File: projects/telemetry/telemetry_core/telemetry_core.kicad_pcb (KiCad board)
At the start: 2 copper layers, 76.2 x 63.5 mm, 59 parts, among them J1 MM_F_RA_20, J2 JST_SM06B-GHS-TB_LF__SN_, J3 CONN_02X03, U1 ATMEGA16M1, U2 TPS560430YF, U3 MCP79511-I_MS, U4 TXB0104PW, U5 LM3480-3.3, U6 MCP2561-E_SN, Y1 Crystal_SMD, Y2 Crystal_32_768kHz

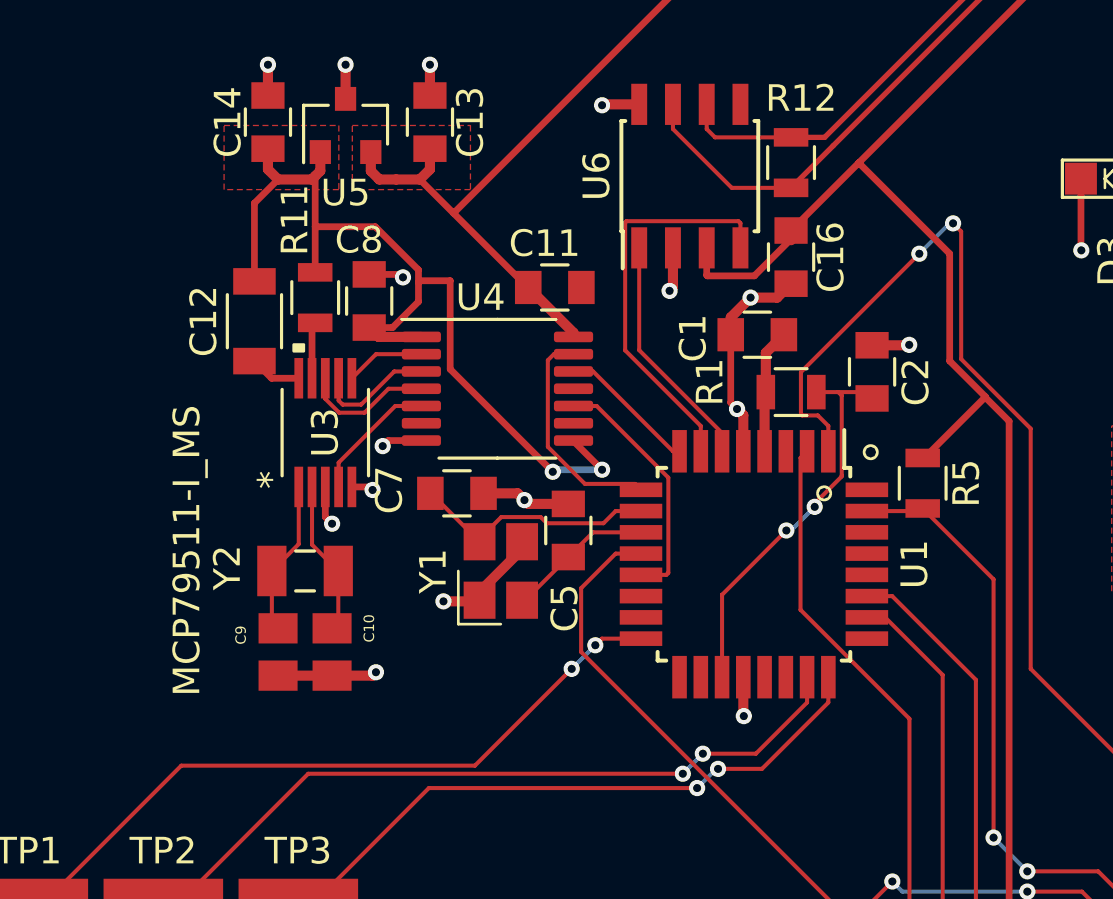
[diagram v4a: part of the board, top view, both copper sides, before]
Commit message: fix: add missing connections, hide label
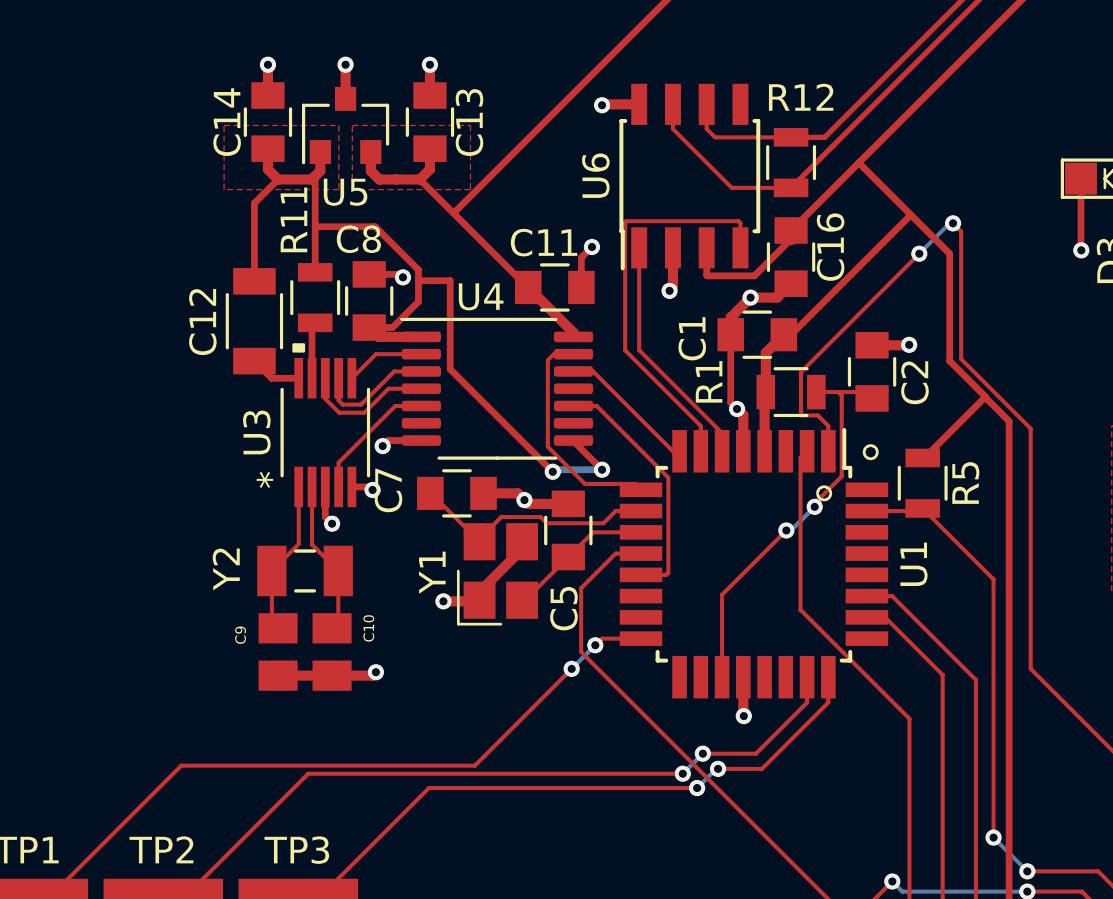
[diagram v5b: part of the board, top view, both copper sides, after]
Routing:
- net +5V: track 137.0 -> 143.6 mm
- net GND: track 98.9 -> 100.6 mm, vias 35 -> 36
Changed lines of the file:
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@@
     (thickness 1.6)
     (drawings 36)
-    (tracks 463)
+    (tracks 469)
     (zones 0)
     (modules 59)
@@
   )
   (setup
-    (last_trace_width 0.1524)
+    (last_trace_width 0.254)
     (user_trace_width 0.254)
     (user_trace_width 0.381)
@@
     (tags "capacitor 0805")
     (attr smd)
-    (fp_text reference C16 (at 0 -1.5 90) (layer F.SilkS)
+    (fp_text reference C16 (at -0.381 -1.524 90) (layer F.SilkS)
       (effects (font (size 1 1) (thickness 0.15)))
     )
@@
       (effects (font (size 1 1) (thickness 0.15)))
     )
-    (fp_text value JST_SM06B-GHS-TB_LF__SN_ (at 9.525 3.84 270) (layer F.Fab)
+    (fp_text value JST_SM06B-GHS-TB_LF__SN_ (at 6.731 -9.652 270) (layer F.Fab)
       (effects (font (size 1 1) (thickness 0.15)))
     )
@@
     (tags "rtc, spi, clock, clk")
     (attr smd)
-    (fp_text reference U3 (at 0 0 90) (layer F.SilkS)
+    (fp_text reference U3 (at 0 -2.54 90) (layer F.SilkS)
       (effects (font (size 1 1) (thickness 0.15)))
     )
-    (fp_text value MCP79511-I_MS (at -4.445 -5.207 90) (layer F.SilkS)
+    (fp_text value MCP79511-I_MS (at -4.445 -5.207 90) (layer F.SilkS) hide
       (effects (font (size 1 1) (thickness 0.15)))
     )
@@
   (via (at 131.699 112.141) (size 0.6096) (drill 0.3048) (layers F.Cu B.Cu) (net 1))
   (segment (start 131.699 113.3) (end 131.699 112.141) (width 0.381) (layer F.Cu) (net 1))
+  (via (at 143.891 118.999) (size 0.6096) (drill 0.3048) (layers F.Cu B.Cu) (net 1))
+  (segment (start 143.494 119.396) (end 143.891 118.999) (width 0.254) (layer F.Cu) (net 1))
+  (segment (start 143.494 120.523) (end 143.494 119.396) (width 0.254) (layer F.Cu) (net 1))
   (segment (start 172.614 102.637) (end 172.593 102.616) (width 0.381) (layer F.Cu) (net 2))
   (segment (start 172.593 112.374) (end 172.614 112.395) (width 0.381) (layer F.Cu) (net 2))
@@
   (segment (start 150.002521 120.086401) (end 148.234401 120.086401) (width 0.254) (layer F.Cu) (net 3))
   (segment (start 151.384 118.38) (end 151.384 118.704922) (width 0.254) (layer F.Cu) (net 3))
-  (segment (start 153.932 115.832) (end 157.353 119.253) (width 0.254) (layer F.Cu) (net 3))
   (segment (start 160.798 108.966) (end 153.932 115.832) (width 0.254) (layer F.Cu) (net 3))
   (segment (start 153.932 115.832) (end 151.384 118.38) (width 0.254) (layer F.Cu) (net 3))
@@
   (segment (start 150.622 105.791) (end 138.684 117.729) (width 0.254) (layer F.Cu) (net 3))
   (segment (start 138.684 117.729) (end 137.414 116.459) (width 0.254) (layer F.Cu) (net 3))
+  (segment (start 151.384 122.301) (end 155.8925 117.7925) (width 0.254) (layer F.Cu) (net 3))
+  (segment (start 151.114 122.301) (end 151.384 122.301) (width 0.254) (layer F.Cu) (net 3))
+  (segment (start 155.8925 117.7925) (end 157.353 119.253) (width 0.254) (layer F.Cu) (net 3))
+  (segment (start 153.932 115.832) (end 155.8925 117.7925) (width 0.254) (layer F.Cu) (net 3))
   (segment (start 154.194 124.46) (end 154.432 124.698) (width 0.1524) (layer F.Cu) (net 4))
   (segment (start 148.787 132.090601) (end 148.787 135.187) (width 0.1524) (layer F.Cu) (net 4))
